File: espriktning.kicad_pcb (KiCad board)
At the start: 2 copper layers, 20 x 75 mm, 40 parts, among them J1 USB_C_Receptacle_USB2.0, J2 Conn_Sensor, J3 Conn_Fan, J4 Conn_01x08, J6 Conn_01x01_Male, J7 Conn_01x01_Male, Q1 2N7002K, Q2 S8050, Q3 S8050, SW1 Reset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

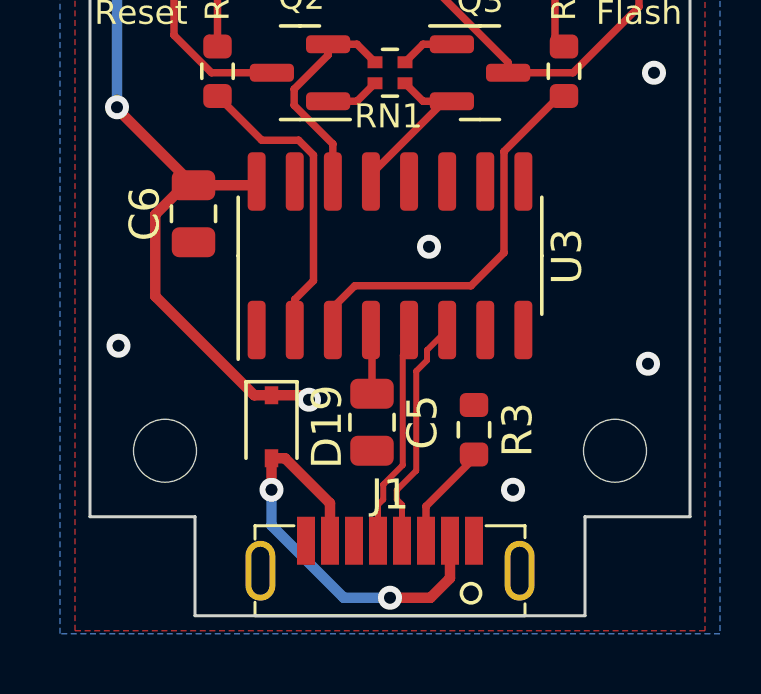
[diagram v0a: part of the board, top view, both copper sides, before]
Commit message: fix usb power
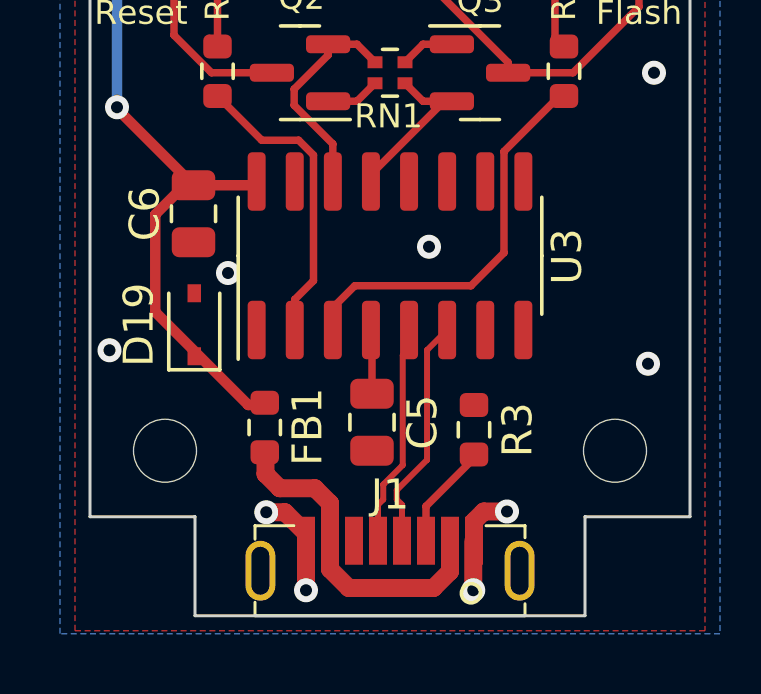
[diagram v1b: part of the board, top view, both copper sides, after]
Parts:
- added FB1: 60R, Resistor_SMD:R_0603_1608Metric, F.Cu at (35.8, 98.7)
- moved D19 4.27 mm to (33.5, 95.3), turned to 90 degrees
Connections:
- D19 pad 2: Net-(D19-Pad2) -> GND
- J1 pad A4: Net-(D19-Pad2) -> /VBUS
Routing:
- net Net-(D19-Pad2): track 14.5 -> 0.00 mm, vias 2 -> 0
- net /VBUS: track 0.00 -> 11.0 mm
- net GND: track 0.00 -> 7.06 mm, vias 46 -> 50
- net +5V: track 122.6 -> 121.5 mm, vias 6 -> 5
